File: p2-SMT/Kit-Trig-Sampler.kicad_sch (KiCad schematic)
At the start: 81 parts, among them J1 START_CV, J10 AUDIO_INR, J11 AUDIO_OUTL, J13 BANK_CV, J14 Eurorack_Power_10pin_Unshroud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, J2 LENGTH_CV, J3 SAMP_CV, J4 PITCH CV, J5 REV_TRIG, J6 PLAY_TRIG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

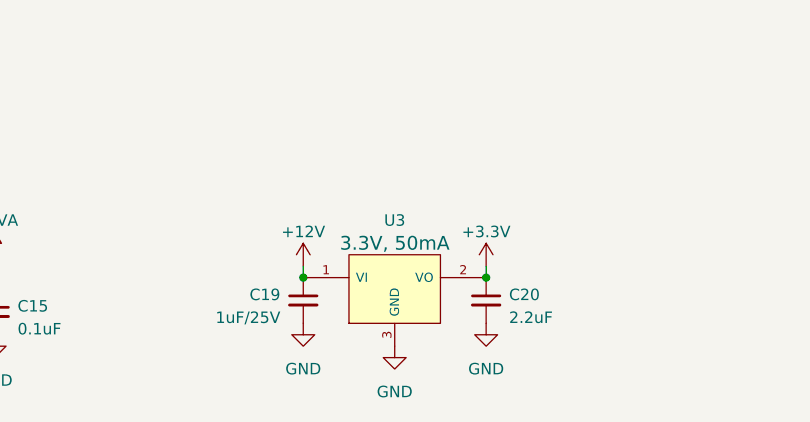
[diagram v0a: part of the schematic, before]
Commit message: p2 SMT: swapped out U3 for different regulator
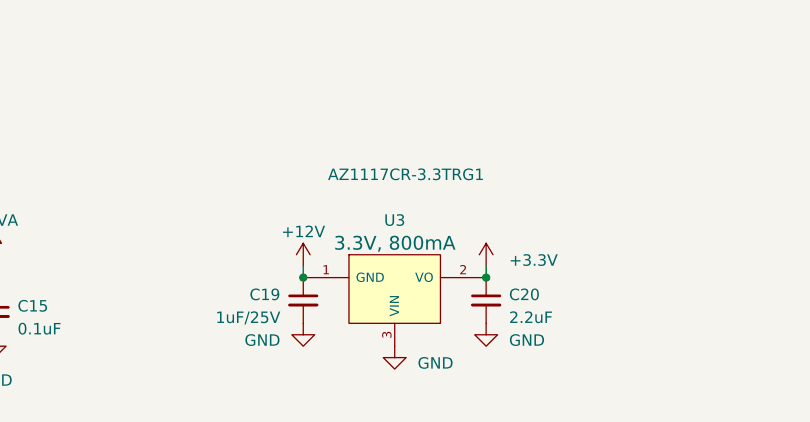
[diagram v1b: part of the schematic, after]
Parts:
- U3: value AP7384-33 -> AZ1117CR-3.3TRG1; footprint 4ms_Package_SOT:SOT23-3_PO132 -> 4ms_Package_SOT:SOT89-3; symbol 4ms_Regulator:AP7384-33 -> 4ms_Regulator:AZ1117CR-3.3TRG1; Display 3.3V, 50mA -> 3.3V, 800mA; Part Number AP7384-33SA-7 -> AZ1117CR-3.3TRG1; Specifications 3.3V Reg. Iout>20mA, Vin>15V -> 3.3V Reg. Iout>20mA, Vin 15V
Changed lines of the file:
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@@
       (effects (font (size 1.27 1.27)) hide)
     )
-    (property "Value" "+3.3V" (at 373.38 375.92 0)
-      (effects (font (size 1.27 1.27)))
+    (property "Value" "+3.3V" (at 375.92 379.095 0)
+      (effects (font (size 1.27 1.27)) (justify left))
     )
     (property "Footprint" "" (at 373.38 379.73 0)
@@
       (effects (font (size 1.27 1.27)) hide)
     )
-    (property "Value" "GND" (at 353.06 391.16 0)
-      (effects (font (size 1.27 1.27)))
+    (property "Value" "GND" (at 350.52 387.985 0)
+      (effects (font (size 1.27 1.27)) (justify right))
     )
     (property "Footprint" "" (at 353.06 386.08 0)
@@
       (effects (font (size 1.27 1.27)) hide)
     )
-    (property "Value" "GND" (at 373.38 391.16 0)
-      (effects (font (size 1.27 1.27)))
+    (property "Value" "GND" (at 375.92 387.985 0)
+      (effects (font (size 1.27 1.27)) (justify left))
     )
     (property "Footprint" "" (at 373.38 386.08 0)
@@
       (effects (font (size 1.27 1.27)) hide)
     )
-    (property "Value" "GND" (at 363.22 393.7 0)
-      (effects (font (size 1.27 1.27)))
+    (property "Value" "GND" (at 365.76 390.525 0)
+      (effects (font (size 1.27 1.27)) (justify left))
     )
     (property "Footprint" "" (at 363.22 388.62 0)
@@
     )
   )
-  (symbol (lib_id "4ms_Regulator:AP7384-33") (at 363.22 382.27 0) (unit 1)
-    (in_bom yes) (on_board yes) (dnp no) (fields_autoplaced)
+  (symbol (lib_id "4ms_Regulator:AZ1117CR-3.3TRG1 ") (at 363.22 382.27 0) (unit 1)
+    (in_bom yes) (on_board yes) (dnp no)
     (property "Reference" "U3" (at 363.22 374.65 0)
       (effects (font (size 1.27 1.27)))
     )
-    (property "Value" "AP7384-33" (at 363.22 374.65 0)
-      (effects (font (size 1.27 1.27)) hide)
+    (property "Value" "AZ1117CR-3.3TRG1 " (at 364.49 369.57 0)
+      (effects (font (size 1.27 1.27)))
     )
-    (property "Footprint" "4ms_Package_SOT:SOT23-3_PO132" (at 365.76 396.24 0)
+    (property "Footprint" "4ms_Package_SOT:SOT89-3" (at 365.76 396.24 0)
       (effects (font (size 1.27 1.27)) hide)
     )
-    (property "Datasheet" "" (at 363.22 382.27 0)
-      (effects (font (size 1.27 1.27)))
+    (property "Datasheet" "https://www.mouser.com/datasheet/2/115/DIOD_S_A0007713706_1-2542909.pdf" (at 365.76 398.78 0)
+      (effects (font (size 1.27 1.27)) hide)
     )
-    (property "Specifications" "3.3V Reg. Iout>20mA, Vin>15V" (at 360.68 390.144 0)
+    (property "Specifications" "3.3V Reg. Iout>20mA, Vin 15V" (at 358.14 401.32 0)
       (effects (font (size 1.27 1.27)) (justify left) hide)
     )
-    (property "Manufacturer" "Diodes Inc." (at 360.68 391.668 0)
+    (property "Manufacturer" "Diodes Inc." (at 360.68 406.4 0)
       (effects (font (size 1.27 1.27)) (justify left) hide)
     )
-    (property "Part Number" "AP7384-33SA-7" (at 360.68 393.192 0)
+    (property "Part Number" "AZ1117CR-3.3TRG1" (at 359.41 403.86 0)
       (effects (font (size 1.27 1.27)) (justify left) hide)
     )
-    (property "Display" "3.3V, 50mA" (at 363.22 377.19 0)
+    (property "Display" "3.3V, 800mA" (at 363.22 377.19 0)
       (effects (font (size 1.524 1.524)))
     )
